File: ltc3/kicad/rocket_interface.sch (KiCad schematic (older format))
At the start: 37 parts

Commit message: LTC3: ignition control adjustments.
1. Renamed "Ignition Control" sheet to "Rocket Interface".  Rocket I/O
   connectors will appear on this sheet.
2. Other minor adjustments to ignition control schematic (signal
   labels, etc.).
3. Added a datasheet for the ignition control circuit's schmitt
   inverter.
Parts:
- removed P?: JP3, symbol CONN_01X02
- added P?: CONN_01X04, symbol CONN_01X04
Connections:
- net GND: now also U?.12
- net ROCKET-READY: now also P?.1 (P1)
- net VSAMPLE renamed VCC_19V
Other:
- note added: "TODO:\n1) Add battery symbol (no footprint)\n2) Do we need a separate charger for the\n ignition battery?"
- note removed: "FIXME: NC?"
- moved on the sheet: P?
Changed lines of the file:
@@
 encoding utf-8
 Sheet 6 8
-Title "LTC3 Ignition Control Board"
-Date "2015-11-14"
-Rev "6.4"
+Title "LTC3 Rocket Interface"
+Date "2015-11-16"
+Rev "A"
 Comp "Portland State Aerospace Society <http://psas.pdx.edu/>"
 Comment1 ""
@@
 L GND #PWR?
 U 1 1 55CD6EA7
-P 1000 4150
-F 0 "#PWR?" H 1000 3900 50  0001 C CNN
-F 1 "GND" H 1000 4000 50  0000 C CNN
-F 2 "" H 1000 4150 60  0000 C CNN
-F 3 "" H 1000 4150 60  0000 C CNN
-	1    1000 4150
+P 1000 4400
+F 0 "#PWR?" H 1000 4150 50  0001 C CNN
+F 1 "GND" H 1000 4250 50  0000 C CNN
+F 2 "" H 1000 4400 60  0000 C CNN
+F 3 "" H 1000 4400 60  0000 C CNN
+	1    1000 4400
 	1    0    0    -1
 $EndComp
@@
 Text Label 2350 8900 2    60   ~ 0
 RR_DELAY
-Text Notes 2150 4000 0    60   ~ 0
-FIXME: NC?
 $Comp
 L CONN_01X02 P?
 U 1 1 56482BE5
+P 10050 7050
+F 0 "P?" H 10050 7200 50  0000 C CNN
+F 1 "IGNITION" V 10150 7050 50  0000 C CNN
+F 2 "" H 10050 7050 60  0000 C CNN
+F 3 "" H 10050 7050 60  0000 C CNN
+	1    10050 7050
+	1    0    0    -1
+$EndComp
+$Comp
+L CONN_01X02 P?
+U 1 1 56482C4A
 P 10050 6450
 F 0 "P?" H 10050 6600 50  0000 C CNN
-F 1 "IGNITION" V 10150 6450 50  0000 C CNN
+F 1 "BATT-IN" V 10150 6450 50  0000 C CNN
 F 2 "" H 10050 6450 60  0000 C CNN
 F 3 "" H 10050 6450 60  0000 C CNN
 	1    10050 6450
-	1    0    0    -1
-$EndComp
-$Comp
-L CONN_01X02 P?
-U 1 1 56482C4A
-P 10050 7050
-F 0 "P?" H 10050 7200 50  0000 C CNN
-F 1 "BATT-IN" V 10150 7050 50  0000 C CNN
-F 2 "" H 10050 7050 60  0000 C CNN
-F 3 "" H 10050 7050 60  0000 C CNN
-	1    10050 7050
 	1    0    0    -1
 $EndComp
@@
 	1    0    0    -1
 $EndComp
+Text Label 9850 7100 2    60   ~ 0
+GND-BATT
+Text Label 9850 7000 2    60   ~ 0
+VCC-IGNITION
 Text Label 9850 6500 2    60   ~ 0
 GND-BATT
 Text Label 9850 6400 2    60   ~ 0
-VCC-IGNITION
-Text Label 9850 7100 2    60   ~ 0
-GND-BATT
-Text Label 9850 7000 2    60   ~ 0
 VCC-BATT
 Text Label 9850 7700 2    60   ~ 0
@@
 $EndComp
 $Comp
-L CONN_01X02 P?
-U 1 1 56490C76
-P 4250 2250
-F 0 "P?" H 4250 2400 50  0000 C CNN
-F 1 "JP3" V 4350 2250 50  0000 C CNN
-F 2 "" H 4250 2250 60  0000 C CNN
-F 3 "" H 4250 2250 60  0000 C CNN
-	1    4250 2250
-	-1   0    0    -1
-$EndComp
-$Comp
 L R R?
 U 1 1 56490E40
@@
 	1    0    0    -1
 $EndComp
-Text Label 4450 2200 0    60   ~ 0
-ROCKET-READY
-Text Label 4450 2300 0    60   ~ 0
-VSAMPLE
 $Comp
 L SN65220DBV U?
@@
 $EndComp
 Wire Wire Line
-	1000 4150 1000 4000
+	1000 4400 1000 4000
 Wire Wire Line
 	1000 4000 1150 4000
@@
 	3400 8900 3950 8900
 Wire Wire Line
-	3950 8650 3950 8900
-Wire Wire Line
-	3950 8900 3950 9150
+	3950 8650 3950 9150
 Wire Wire Line
 	3950 8650 4400 8650
@@
 	10150 2300 9650 2300
 Wire Wire Line
-	10250 2550 11200 2550
-Wire Wire Line
-	11200 2550 11500 2550
+	10250 2550 11500 2550
 Wire Wire Line
 	9650 3050 10950 3050
@@
 	10950 3050 10950 1300
 Wire Wire Line
-	10850 2750 11400 2750
-Wire Wire Line
-	11400 2750 11500 2750
+	10850 2750 11500 2750
 Wire Wire Line
 	1350 2300 1350 2050
@@
 Connection ~ 11200 2550
 Wire Wire Line
-	11200 3400 11200 3500
-Wire Wire Line
-	11200 3500 11200 3600
+	11200 3400 11200 3600
 Wire Wire Line
 	11400 3400 11400 3500
@@
 Connection ~ 11200 3500
 Wire Wire Line
-	15050 3200 15050 3300
-Wire Wire Line
-	15050 3300 15050 3400
+	15050 3200 15050 3400
 Wire Wire Line
 	15400 3200 15400 3300
@@
 Connection ~ 15050 3300
 Wire Wire Line
-	12700 2650 13500 2650
-Wire Wire Line
-	13500 2650 13800 2650
-Wire Wire Line
-	13800 2650 13900 2650
+	12700 2650 13900 2650
 Wire Wire Line
 	13900 2900 13800 2900
@@
 	15050 2650 15050 2900
 Wire Wire Line
-	14200 2650 14300 2650
-Wire Wire Line
-	14300 2650 14650 2650
-Wire Wire Line
-	14650 2650 15050 2650
-Wire Wire Line
-	15050 2650 15400 2650
-Wire Wire Line
-	15400 2650 15550 2650
+	14200 2650 15550 2650
 Wire Wire Line
 	14200 2900 14300 2900
@@
 	2350 8900 2500 8900
 Wire Wire Line
-	9850 6500 9700 6500
-Wire Wire Line
-	9700 6500 9700 7100
-Wire Wire Line
-	9700 7100 9700 7700
-Wire Wire Line
-	9700 7100 9850 7100
+	9850 7100 9700 7100
+Wire Wire Line
+	9700 6500 9850 6500
 Wire Wire Line
 	9700 7700 9850 7700
-Connection ~ 9700 7100
-Wire Wire Line
-	7250 9200 7250 9300
-Wire Wire Line
-	7250 9300 7250 9400
+Wire Wire Line
+	7250 9200 7250 9400
 Wire Wire Line
 	7800 8800 7800 9300
@@
 	8500 2050 8500 2300
 Wire Wire Line
-	8000 2300 8500 2300
-Wire Wire Line
-	8500 2300 8750 2300
+	8000 2300 8750 2300
 Connection ~ 8500 2300
 Wire Wire Line
-	7150 2400 7150 2650
-Wire Wire Line
-	7150 2650 7150 2800
+	7150 2400 7150 2800
 Wire Wire Line
 	7150 2400 7400 2400
@@
 	5900 2350 5900 2200
 Wire Wire Line
-	5750 2200 5900 2200
-Wire Wire Line
-	5900 2200 6150 2200
-Wire Wire Line
-	6150 2200 7400 2200
-Wire Wire Line
-	5450 2200 4450 2200
+	5750 2200 7400 2200
 Wire Wire Line
 	5900 2800 5900 2650
@@
 Connection ~ 6150 2200
 Wire Wire Line
-	8050 4800 8050 4700
-Wire Wire Line
-	8050 4700 8050 4600
+	8050 4600 8050 4800
 Wire Wire Line
 	8400 4600 8400 4700
@@
 Connection ~ 8050 4700
 Wire Wire Line
-	8050 4300 8050 4150
-Wire Wire Line
-	8050 4150 8050 4100
-Wire Wire Line
-	8050 4100 8050 4000
+	8050 4000 8050 4300
 Wire Wire Line
 	7400 4100 8050 4100
 Connection ~ 8050 4100
 Wire Wire Line
-	8400 3050 8400 4150
-Wire Wire Line
-	8400 4150 8400 4300
+	8400 3050 8400 4300
 Wire Wire Line
 	8400 4150 8050 4150
 Connection ~ 8050 4150
-Wire Wire Line
-	4450 2300 5400 2300
 Wire Wire Line
 	5400 2300 5400 3550
@@
 $EndComp
 Wire Wire Line
-	5300 8650 7250 8650
-Wire Wire Line
-	7250 8650 7500 8650
+	5300 8650 7500 8650
 $Comp
 L RELAY_SPDT K?
@@
 $EndComp
 Wire Wire Line
-	6200 7700 6850 7700
-Wire Wire Line
-	6200 6700 6200 7300
-Wire Wire Line
-	6200 7300 6200 7700
-Wire Wire Line
-	6200 7300 6350 7300
+	5950 7700 6850 7700
+Wire Wire Line
+	5950 6200 5950 7700
+Wire Wire Line
+	5950 7300 6350 7300
 Wire Wire Line
 	7150 7700 7800 7700
 Wire Wire Line
-	7800 7300 7800 7700
-Wire Wire Line
-	7800 7700 7800 8400
+	7800 7300 7800 8400
 Wire Wire Line
 	7800 7300 7650 7300
@@
 L VCC #PWR?
 U 1 1 564927D6
-P 6200 6700
-F 0 "#PWR?" H 6200 6550 50  0001 C CNN
-F 1 "VCC" H 6200 6850 50  0000 C CNN
-F 2 "" H 6200 6700 60  0000 C CNN
-F 3 "" H 6200 6700 60  0000 C CNN
-	1    6200 6700
-	1    0    0    -1
-$EndComp
-Connection ~ 6200 7300
-Text Label 6050 7050 2    60   ~ 0
-VCC-BATT
-Wire Wire Line
-	6050 7050 6350 7050
-Wire Wire Line
-	7650 7000 7800 7000
-Wire Wire Line
-	7800 7000 7800 6400
-Wire Wire Line
-	7800 6400 9850 6400
+P 5950 6200
+F 0 "#PWR?" H 5950 6050 50  0001 C CNN
+F 1 "VCC" H 5950 6350 50  0000 C CNN
+F 2 "" H 5950 6200 60  0000 C CNN
+F 3 "" H 5950 6200 60  0000 C CNN
+	1    5950 6200
+	1    0    0    -1
+$EndComp
+Connection ~ 5950 7300
 Wire Wire Line
 	7650 7100 7950 7100
@@
 	1    0    0    -1
 $EndComp
+Wire Wire Line
+	6350 7050 6200 7050
+Wire Wire Line
+	7650 7000 9850 7000
+Wire Wire Line
+	9700 6500 9700 7700
+Connection ~ 9700 7100
+Wire Wire Line
+	6200 7050 6200 6400
+Wire Wire Line
+	6200 6400 9850 6400
+Text Notes 12300 9050 0    100  ~ 0
+TODO:\n1) Add battery symbol (no footprint)\n2) Do we need a separate charger for the\n   ignition battery?
+Wire Wire Line
+	2050 4000 2250 4000
+Wire Wire Line
+	2250 4000 2250 4300
+Wire Wire Line
+	2250 4300 1000 4300
+Connection ~ 1000 4300
+Text HLabel 5200 2300 0    60   Input ~ 0
+VCC_19V
+Wire Wire Line
+	5450 2200 5200 2200
+Wire Wire Line
+	5400 2300 5200 2300
+Text HLabel 1450 5700 2    60   Output ~ 0
+ROCKET-READY
+Wire Wire Line
+	1450 5700 1200 5700
+Text Label 1350 5700 1    60   ~ 0
+ROCKET-READY
+$Comp
+L CONN_01X04 P?
+U 1 1 564BF3B4
+P 1000 5850
+F 0 "P?" H 1000 6100 50  0000 C CNN
+F 1 "CONN_01X04" V 1100 5850 50  0000 C CNN
+F 2 "" H 1000 5850 60  0000 C CNN
+F 3 "" H 1000 5850 60  0000 C CNN
+	1    1000 5850
+	-1   0    0    -1
+$EndComp
+Text Label 5200 2200 2    60   ~ 0
+ROCKET-READY
 $EndSCHEMATC

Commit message: LTC3: Tidied up rocket interface schematic.
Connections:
- net VCC_19V: now also R?.2; no longer R?.1
- net at C?.1, R?.1, U?.3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: now also R?.1; no longer R?.2
- net BATT-CHARGE-RELAY renamed IGN_BATT_CHG
- net GND-BATT renamed GND_IGN_BATT
- net RR_DELAY: no longer names the net of C?.1, C?.1, R?.1, R?.1, R?.1, U?.5
- net VCC-BATT renamed IGN_BATT
- net VCC-IGNITION renamed IGNITION
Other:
- note added: "+1.2V"
- note added: "+5V"
- note added: "Delay (5s)"
- note added: "Ignition/Battery Control"
- note added: "Input Logic"
- note added: "TODO:\n* Select appropriate component values.\n\nQUESTIONS:\n* Keep the "test" jumpers?\n* Do we need to integrate a charger for the ignition\n battery?\n* Where's the launch/ignition signal?\n* What's the purpose of the TVS on the\n input signals? It clamps at 7V, more than enough\n to look like a genuine high input."
- note removed: "Five Second Charge Time"
- note removed: "TODO:\n1) Add battery symbol (no footprint)\n2) Do we need a separate charger for the\n ignition battery?"
- moved on the sheet: C?, D?, K?, P?, Q?, R?, U?, U?A, U?B, U?C, U?D, U?E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

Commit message: Minor progress on battery balance schematic.
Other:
- note added: "TODO:\n* Select appropriate component values.\n\nQUESTIONS:\n* Keep the "test" jumpers?\n* Do we need to integrate a charger for the ignition\n battery?\n* Where's the launch/ignition signal?\n* What's the purpose of the TVS on the\n input signals? It clamps at 7V, more than enough\n to look like a genuine high input.\n* What's the purpose of the extra resistor and cap.\n in the delay stage? Post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"
- note removed: "FIXME: "NP" values?"
- note removed: "TODO:\n* Select appropriate component values.\n\nQUESTIONS:\n* Keep the "test" jumpers?\n* Do we need to integrate a charger for the ignition\n battery?\n* Where's the launch/ignition signal?\n* What's the purpose of the TVS on the\n input signals? It clamps at 7V, more than enough\n to look like a genuine high input."
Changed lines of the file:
@@
 	1    0    0    -1
 $EndComp
-Text Notes 1800 9250 0    60   ~ 0
-FIXME: "NP" values?
 $Comp
 L GND #PWR?
@@
 $EndComp
 $Comp
-L GND #PWR?
-U 1 1 5648B405
-P 9950 3300
-F 0 "#PWR?" H 9950 3050 50  0001 C CNN
-F 1 "GND" H 9950 3150 50  0000 C CNN
-F 2 "" H 9950 3300 60  0000 C CNN
-F 3 "" H 9950 3300 60  0000 C CNN
-	1    9950 3300
-	1    0    0    -1
-$EndComp
-$Comp
 L R R?
 U 1 1 5648F319
@@
 $Comp
 L VCC #PWR?
-U 1 1 56487DF9
-P 9950 2200
-F 0 "#PWR?" H 9950 2050 50  0001 C CNN
-F 1 "VCC" H 9950 2350 50  0000 C CNN
-F 2 "" H 9950 2200 60  0000 C CNN
-F 3 "" H 9950 2200 60  0000 C CNN
-	1    9950 2200
-	1    0    0    -1
-$EndComp
-$Comp
-L VCC #PWR?
 U 1 1 56488625
 P 14700 2150
@@
 $EndComp
 Text Notes 12250 9150 0    100  ~ 0
-TODO:\n* Select appropriate component values.\n\nQUESTIONS:\n* Keep the "test" jumpers?\n* Do we need to integrate a charger for the ignition\n  battery?\n* Where's the launch/ignition signal?\n* What's the purpose of the TVS on the\n  input signals?  It clamps at 7V, more than enough\n  to look like a genuine high input.
+TODO:\n* Select appropriate component values.\n\nQUESTIONS:\n* Keep the "test" jumpers?\n* Do we need to integrate a charger for the ignition\n  battery?\n* Where's the launch/ignition signal?\n* What's the purpose of the TVS on the\n  input signals?  It clamps at 7V, more than enough\n  to look like a genuine high input.\n* What's the purpose of the extra resistor and cap.\n  in the delay stage?  Post-assembly adjustment?
 Text HLabel 1900 3950 0    60   Input ~ 0
 VCC_19V
@@
 Wire Wire Line
 	8200 8300 8200 8550
-Wire Wire Line
-	9950 2200 9950 2350
-Wire Wire Line
-	9950 3300 9950 3150
 Connection ~ 8200 8300
 Wire Wire Line

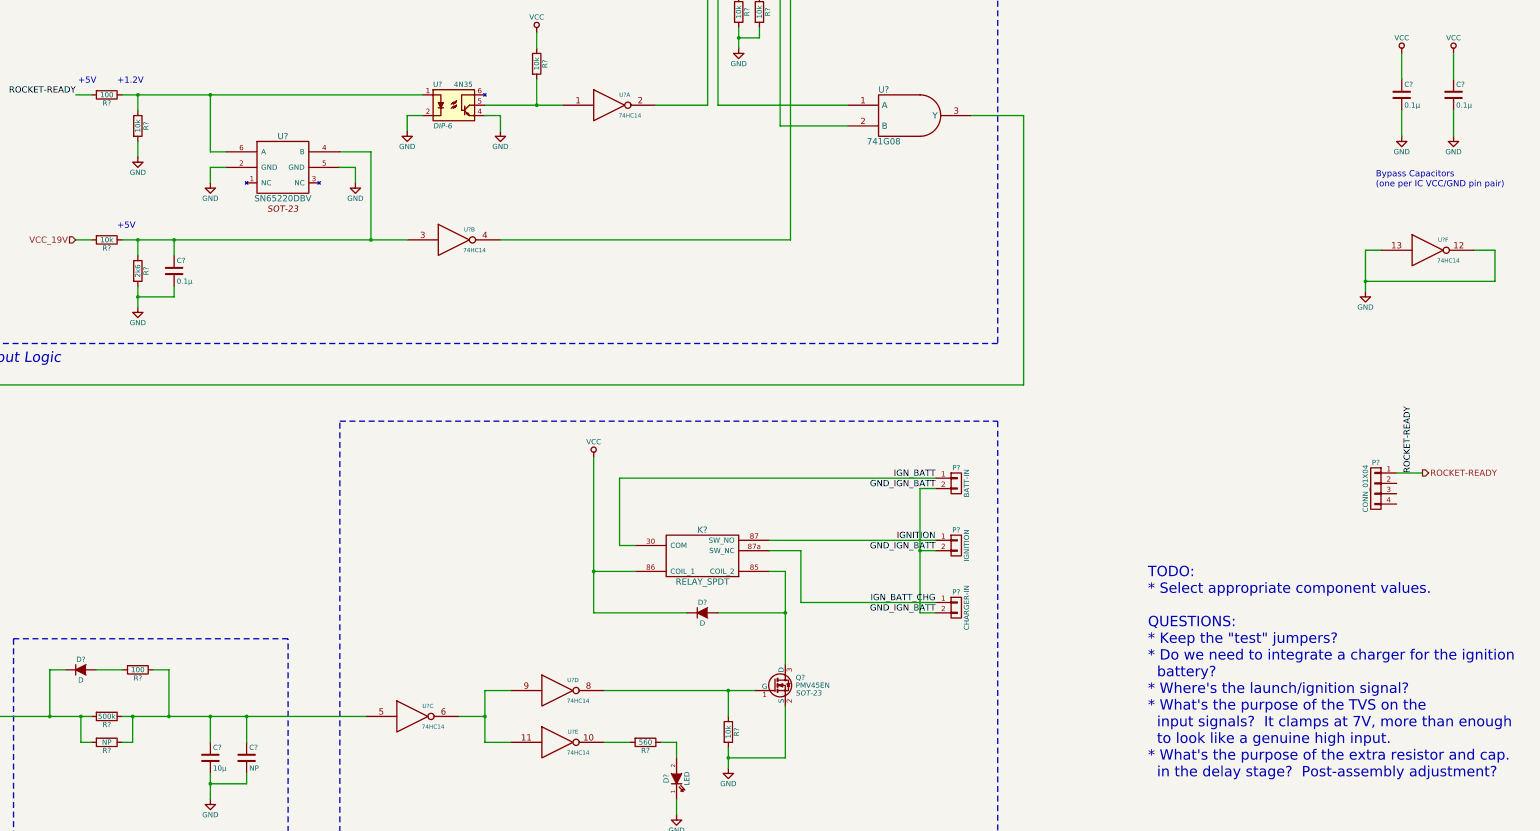
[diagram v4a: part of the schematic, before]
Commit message: LTC3: Schematic corrections.
1. Replaced ignition schematic Schmitt trigger symbols with symbols
   that actually include the Schmitt squiggle.
2. Annotated DC detection circuit on battery management schematic;
   removed related entry from TODO list.
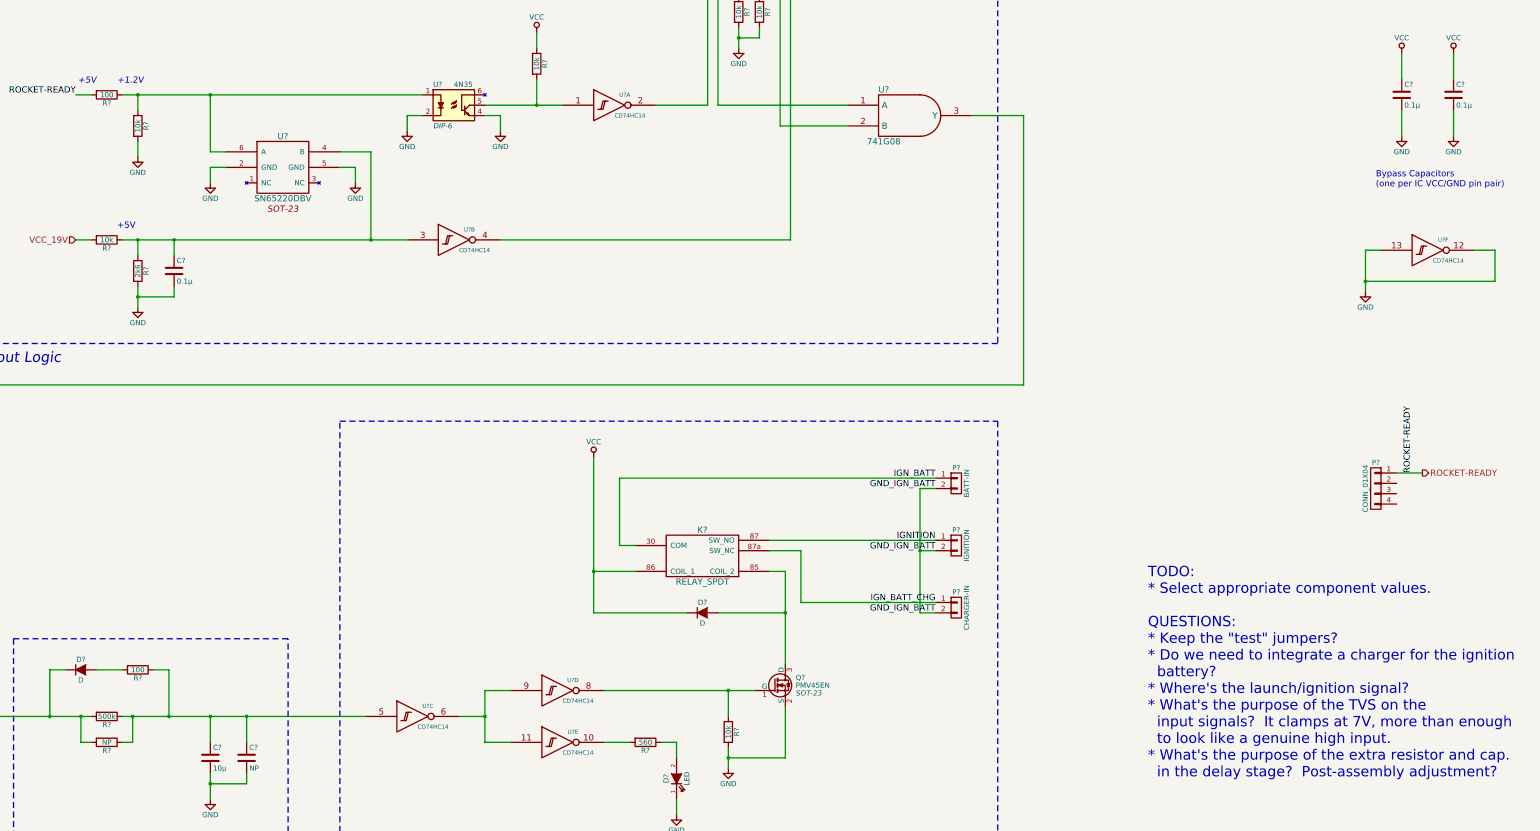
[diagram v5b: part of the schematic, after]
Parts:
- removed U? (x6): 74HC14, symbol 74HC14
- added U? (x6): CD74HC14, symbol CD74HC14
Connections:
- net GND: now also U?.12, U?.13, U?.7 (GND), U?.7 (GND), U?.7 (GND), U?.7 (GND), U?.7 (GND), U?.7 (GND)
- net VCC: now also U?.14 (VCC), U?.14 (VCC), U?.14 (VCC), U?.14 (VCC), U?.14 (VCC), U?.14 (VCC)
- net at R?.2, U?.5: now also U?.1
- net at P?.1 (P1): now also U?.2
- net at C?.1, R?.1, R?.1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: now also U?.3
- net at P?.2 (P2): now also U?.4
- net at C?.1, C?.1, R?.1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: now also U?.5
- net at Q?.1 (G), R?.1: now also U?.8
- net at R?.2: now also U?.10
- new net: U?.11, U?.6, U?.9
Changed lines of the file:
@@
 LIBS:SNx52x0
 LIBS:switches
+LIBS:CD74HC14
 LIBS:Launch_Tower_Computer_III-cache
 EELAYER 25 0
@@
 $Descr B 17000 11000
 encoding utf-8
-Sheet 6 8
+Sheet 5 8
 Title "LTC3 Rocket Interface"
 Date "2015-11-20"
@@
 Comment4 ""
 $EndDescr
-$Comp
-L 74HC14 U?
-U 1 1 55CD6A42
-P 7050 2650
-F 0 "U?" H 7200 2750 40  0000 C CNN
-F 1 "74HC14" H 7250 2550 40  0000 C CNN
-F 2 "" H 7050 2650 60  0000 C CNN
-F 3 "" H 7050 2650 60  0000 C CNN
-	1    7050 2650
-	1    0    0    -1
-$EndComp
-$Comp
-L 74HC14 U?
-U 2 1 55CD6A93
-P 5550 3950
-F 0 "U?" H 5700 4050 40  0000 C CNN
-F 1 "74HC14" H 5750 3850 40  0000 C CNN
-F 2 "" H 5550 3950 60  0000 C CNN
-F 3 "" H 5550 3950 60  0000 C CNN
-	2    5550 3950
-	1    0    0    -1
-$EndComp
-$Comp
-L 74HC14 U?
-U 3 1 55CD6B0C
-P 5150 8550
-F 0 "U?" H 5300 8650 40  0000 C CNN
-F 1 "74HC14" H 5350 8450 40  0000 C CNN
-F 2 "" H 5150 8550 60  0000 C CNN
-F 3 "" H 5150 8550 60  0000 C CNN
-	3    5150 8550
-	1    0    0    -1
-$EndComp
-$Comp
-L 74HC14 U?
-U 4 1 55CD6B50
-P 6550 8300
-F 0 "U?" H 6700 8400 40  0000 C CNN
-F 1 "74HC14" H 6750 8200 40  0000 C CNN
-F 2 "" H 6550 8300 60  0000 C CNN
-F 3 "" H 6550 8300 60  0000 C CNN
-	4    6550 8300
-	1    0    0    -1
-$EndComp
-$Comp
-L 74HC14 U?
-U 5 1 55CD6BF3
-P 6550 8800
-F 0 "U?" H 6700 8900 40  0000 C CNN
-F 1 "74HC14" H 6750 8700 40  0000 C CNN
-F 2 "" H 6550 8800 60  0000 C CNN
-F 3 "" H 6550 8800 60  0000 C CNN
-	5    6550 8800
-	1    0    0    -1
-$EndComp
-$Comp
-L 74HC14 U?
-U 6 1 55CD6DA4
-P 14950 4050
-F 0 "U?" H 15100 4150 40  0000 C CNN
-F 1 "74HC14" H 15150 3950 40  0000 C CNN
-F 2 "" H 14950 4050 60  0000 C CNN
-F 3 "" H 14950 4050 60  0000 C CNN
-	6    14950 4050
-	1    0    0    -1
-$EndComp
 $Comp
 L GND #PWR?
@@
 Wire Wire Line
 	1050 8550 2050 8550
-Text Notes 2100 2450 2    60   ~ 0
+Text Notes 2100 2450 2    60   Italic 0
 +5V
-Text Notes 2300 2450 0    60   ~ 0
+Text Notes 2300 2450 0    60   Italic 0
 +1.2V
 Text Notes 2300 3850 0    60   ~ 0
@@
 Wire Wire Line
 	8500 2000 8300 2000
+$Comp
+L CD74HC14 U?
+U 1 1 5650FE70
+P 7050 2650
+F 0 "U?" H 7200 2750 40  0000 C CNN
+F 1 "CD74HC14" H 7250 2550 40  0000 C CNN
+F 2 "" H 7050 2650 60  0000 C CNN
+F 3 "" H 7050 2650 60  0000 C CNN
+	1    7050 2650
+	1    0    0    -1
+$EndComp
+$Comp
+L CD74HC14 U?
+U 2 1 56510E08
+P 5550 3950
+F 0 "U?" H 5700 4050 40  0000 C CNN
+F 1 "CD74HC14" H 5750 3850 40  0000 C CNN
+F 2 "" H 5550 3950 60  0000 C CNN
+F 3 "" H 5550 3950 60  0000 C CNN
+	2    5550 3950
+	1    0    0    -1
+$EndComp
+$Comp
+L CD74HC14 U?
+U 3 1 56512200
+P 5150 8550
+F 0 "U?" H 5300 8650 40  0000 C CNN
+F 1 "CD74HC14" H 5350 8450 40  0000 C CNN
+F 2 "" H 5150 8550 60  0000 C CNN
+F 3 "" H 5150 8550 60  0000 C CNN
+	3    5150 8550
+	1    0    0    -1
+$EndComp
+$Comp
+L CD74HC14 U?
+U 4 1 56512296
+P 6550 8300
+F 0 "U?" H 6700 8400 40  0000 C CNN
+F 1 "CD74HC14" H 6750 8200 40  0000 C CNN
+F 2 "" H 6550 8300 60  0000 C CNN
+F 3 "" H 6550 8300 60  0000 C CNN
+	4    6550 8300
+	1    0    0    -1
+$EndComp
+$Comp
+L CD74HC14 U?
+U 5 1 5651237A
+P 6550 8800
+F 0 "U?" H 6700 8900 40  0000 C CNN
+F 1 "CD74HC14" H 6750 8700 40  0000 C CNN
+F 2 "" H 6550 8800 60  0000 C CNN
+F 3 "" H 6550 8800 60  0000 C CNN
+	5    6550 8800
+	1    0    0    -1
+$EndComp
+$Comp
+L CD74HC14 U?
+U 6 1 5651300D
+P 14950 4050
+F 0 "U?" H 15100 4150 40  0000 C CNN
+F 1 "CD74HC14" H 15150 3950 40  0000 C CNN
+F 2 "" H 14950 4050 60  0000 C CNN
+F 3 "" H 14950 4050 60  0000 C CNN
+	6    14950 4050
+	1    0    0    -1
+$EndComp
 $EndSCHEMATC

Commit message: LTC3: Converted hierarchical power pins to global power nodes.
This eliminates the need to manually route power from one top-level
sheet to another.
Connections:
- net VCC: no longer C?.1, C?.1, D?.1 (K), K?.86 (COIL_1), R?.1
- net VCC_19V renamed +19V
- new net +5V: C?.1, C?.1, D?.1 (K), K?.86 (COIL_1), R?.1
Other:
- note added: "Bypass Capacitors\n(one per IC VCC)"
- note added: "Spare Schmitt Inverter"
- note added: "VCC for CD74HC14"
- note removed: "Bypass Capacitors\n(one per IC VCC/GND pin pair)"
